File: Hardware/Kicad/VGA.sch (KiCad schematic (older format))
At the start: 9 parts, among them P701 VGA OUT

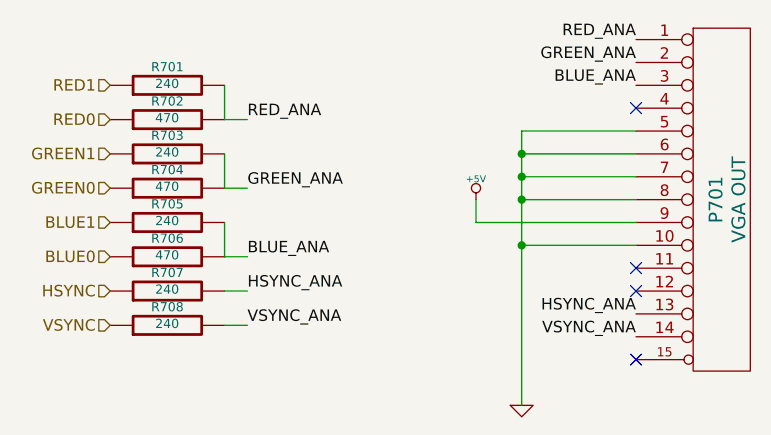
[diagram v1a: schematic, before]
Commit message: Schematic Rev. 11
Added LEDs; some minor other modifications
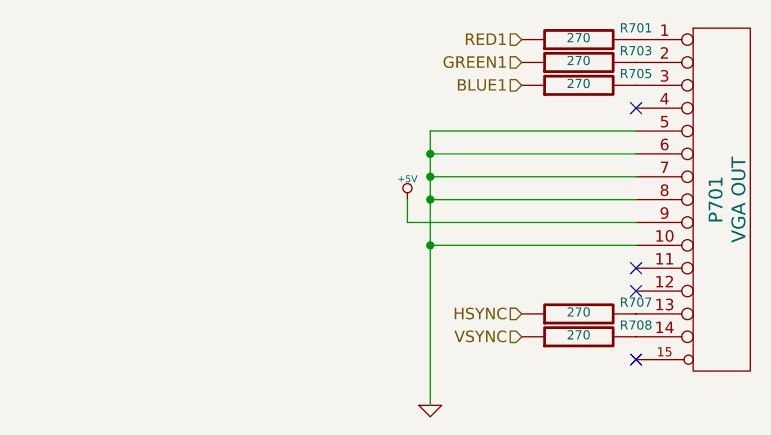
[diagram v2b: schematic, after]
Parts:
- removed R702, R704, R706: 470, ~, symbol R
- R701, R703, R705, R707, R708: value 240 -> 270
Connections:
- net BLUE_ANA: no longer names the net of P701.3 (P3), R705.2
- net GREEN_ANA: no longer names the net of P701.2 (P2), R703.2
- net HSYNC_ANA: no longer names the net of P701.13 (P13), R707.2
- net RED_ANA: no longer names the net of P701.1 (P1), R701.2
- net VSYNC_ANA: no longer names the net of P701.14 (P14), R708.2
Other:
- moved on the sheet: R701, R703, R705, R707, R708
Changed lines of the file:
@@
 Title "Propeddle"
 Date "18 apr 2014"
-Rev "10"
+Rev "11"
 Comp "(C) 2014 Jac Goudsmit"
 Comment1 "Software-Defined 6502 Computer"
@@
 	1    0    0    -1
 $EndComp
-Text Label 6750 3100 2    50   ~ 0
-RED_ANA
-Text Label 6750 3200 2    50   ~ 0
-GREEN_ANA
-Text Label 6750 3300 2    50   ~ 0
-BLUE_ANA
 $Comp
-L GND #PWR031
+L GND #PWR033
 U 1 1 534358FB
-P 6250 4700
-F 0 "#PWR031" H 6250 4700 30  0001 C CNN
-F 1 "GND" H 6250 4630 30  0001 C CNN
-F 2 "" H 6250 4700 60  0000 C CNN
-F 3 "" H 6250 4700 60  0000 C CNN
-	1    6250 4700
+P 5850 4700
+F 0 "#PWR033" H 5850 4700 30  0001 C CNN
+F 1 "GND" H 5850 4630 30  0001 C CNN
+F 2 "" H 5850 4700 60  0000 C CNN
+F 3 "" H 5850 4700 60  0000 C CNN
+	1    5850 4700
 	1    0    0    -1
 $EndComp
 $Comp
-L +5V #PWR032
+L +5V #PWR034
 U 1 1 5343590A
-P 6050 3800
-F 0 "#PWR032" H 6050 3890 20  0001 C CNN
-F 1 "+5V" H 6050 3890 30  0000 C CNN
-F 2 "" H 6050 3800 60  0000 C CNN
-F 3 "" H 6050 3800 60  0000 C CNN
-	1    6050 3800
+P 5750 3800
+F 0 "#PWR034" H 5750 3890 20  0001 C CNN
+F 1 "+5V" H 5750 3890 30  0000 C CNN
+F 2 "" H 5750 3800 60  0000 C CNN
+F 3 "" H 5750 3800 60  0000 C CNN
+	1    5750 3800
 	1    0    0    -1
 $EndComp
-Text Label 6750 4300 2    50   ~ 0
-HSYNC_ANA
-Text Label 6750 4400 2    50   ~ 0
-VSYNC_ANA
 $Comp
 L R R701
 U 1 1 5343593B
-P 4700 3300
-F 0 "R701" V 4780 3300 40  0000 C CNN
-F 1 "240" V 4707 3301 40  0000 C CNN
-F 2 "~" V 4630 3300 30  0000 C CNN
-F 3 "~" H 4700 3300 30  0000 C CNN
-	1    4700 3300
+P 6500 3100
+F 0 "R701" V 6550 2850 40  0000 C CNN
+F 1 "270" V 6507 3101 40  0000 C CNN
+F 2 "~" V 6430 3100 30  0000 C CNN
+F 3 "~" H 6500 3100 30  0000 C CNN
+	1    6500 3100
 	0    -1   -1   0
 $EndComp
@@
 L R R703
 U 1 1 5343594D
-P 4700 3600
-F 0 "R703" V 4780 3600 40  0000 C CNN
-F 1 "240" V 4707 3601 40  0000 C CNN
-F 2 "~" V 4630 3600 30  0000 C CNN
-F 3 "~" H 4700 3600 30  0000 C CNN
-	1    4700 3600
+P 6500 3200
+F 0 "R703" V 6550 2950 40  0000 C CNN
+F 1 "270" V 6507 3201 40  0000 C CNN
+F 2 "~" V 6430 3200 30  0000 C CNN
+F 3 "~" H 6500 3200 30  0000 C CNN
+	1    6500 3200
 	0    -1   -1   0
 $EndComp
@@
 L R R705
 U 1 1 53435953
-P 4700 3900
-F 0 "R705" V 4780 3900 40  0000 C CNN
-F 1 "240" V 4707 3901 40  0000 C CNN
-F 2 "~" V 4630 3900 30  0000 C CNN
-F 3 "~" H 4700 3900 30  0000 C CNN
-	1    4700 3900
-	0    -1   -1   0
-$EndComp
-$Comp
-L R R704
-U 1 1 53435963
-P 4700 3750
-F 0 "R704" V 4780 3750 40  0000 C CNN
-F 1 "470" V 4707 3751 40  0000 C CNN
-F 2 "~" V 4630 3750 30  0000 C CNN
-F 3 "~" H 4700 3750 30  0000 C CNN
-	1    4700 3750
-	0    -1   -1   0
-$EndComp
-$Comp
-L R R702
-U 1 1 5343596E
-P 4700 3450
-F 0 "R702" V 4780 3450 40  0000 C CNN
-F 1 "470" V 4707 3451 40  0000 C CNN
-F 2 "~" V 4630 3450 30  0000 C CNN
-F 3 "~" H 4700 3450 30  0000 C CNN
-	1    4700 3450
-	0    -1   -1   0
-$EndComp
-$Comp
-L R R706
-U 1 1 53435974
-P 4700 4050
-F 0 "R706" V 4780 4050 40  0000 C CNN
-F 1 "470" V 4707 4051 40  0000 C CNN
-F 2 "~" V 4630 4050 30  0000 C CNN
-F 3 "~" H 4700 4050 30  0000 C CNN
-	1    4700 4050
+P 6500 3300
+F 0 "R705" V 6550 3050 40  0000 C CNN
+F 1 "270" V 6507 3301 40  0000 C CNN
+F 2 "~" V 6430 3300 30  0000 C CNN
+F 3 "~" H 6500 3300 30  0000 C CNN
+	1    6500 3300
 	0    -1   -1   0
 $EndComp
@@
 L R R707
 U 1 1 5343597A
-P 4700 4200
-F 0 "R707" V 4780 4200 40  0000 C CNN
-F 1 "240" V 4707 4201 40  0000 C CNN
-F 2 "~" V 4630 4200 30  0000 C CNN
-F 3 "~" H 4700 4200 30  0000 C CNN
-	1    4700 4200
+P 6500 4300
+F 0 "R707" V 6550 4050 40  0000 C CNN
+F 1 "270" V 6507 4301 40  0000 C CNN
+F 2 "~" V 6430 4300 30  0000 C CNN
+F 3 "~" H 6500 4300 30  0000 C CNN
+	1    6500 4300
 	0    -1   -1   0
 $EndComp
@@
 L R R708
 U 1 1 53435980
-P 4700 4350
-F 0 "R708" V 4780 4350 40  0000 C CNN
-F 1 "240" V 4707 4351 40  0000 C CNN
-F 2 "~" V 4630 4350 30  0000 C CNN
-F 3 "~" H 4700 4350 30  0000 C CNN
-	1    4700 4350
+P 6500 4400
+F 0 "R708" V 6550 4150 40  0000 C CNN
+F 1 "270" V 6507 4401 40  0000 C CNN
+F 2 "~" V 6430 4400 30  0000 C CNN
+F 3 "~" H 6500 4400 30  0000 C CNN
+	1    6500 4400
 	0    -1   -1   0
 $EndComp
 Wire Wire Line
-	6750 3500 6250 3500
+	6750 3500 5850 3500
 Wire Wire Line
-	6250 3500 6250 4700
+	5850 3500 5850 4700
 Wire Wire Line
-	6750 4000 6250 4000
-Connection ~ 6250 4000
+	6750 4000 5850 4000
+Connection ~ 5850 4000
 Wire Wire Line
-	6050 3800 6050 3900
+	5750 3800 5750 3900
 Wire Wire Line
-	6050 3900 6750 3900
+	5750 3900 6750 3900
 Wire Wire Line
-	6250 3600 6750 3600
-Connection ~ 6250 3600
+	5850 3600 6750 3600
+Connection ~ 5850 3600
 Wire Wire Line
-	6250 3700 6750 3700
-Connection ~ 6250 3700
+	5850 3700 6750 3700
+Connection ~ 5850 3700
 Wire Wire Line
-	6750 3800 6250 3800
-Connection ~ 6250 3800
-Wire Wire Line
-	4950 3300 4950 3450
-Wire Wire Line
-	4950 3450 5050 3450
-Wire Wire Line
-	4950 3600 4950 3750
-Wire Wire Line
-	4950 3750 5050 3750
-Wire Wire Line
-	4950 3900 4950 4050
-Wire Wire Line
-	4950 4050 5050 4050
-Text Label 5050 3450 0    50   ~ 0
-RED_ANA
-Text Label 5050 3750 0    50   ~ 0
-GREEN_ANA
-Text Label 5050 4050 0    50   ~ 0
-BLUE_ANA
-Wire Wire Line
-	4950 4200 5050 4200
-Wire Wire Line
-	4950 4350 5050 4350
-Text Label 5050 4200 0    50   ~ 0
-HSYNC_ANA
-Text Label 5050 4350 0    50   ~ 0
-VSYNC_ANA
-Text HLabel 4450 3300 0    50   Input ~ 0
+	6750 3800 5850 3800
+Connection ~ 5850 3800
+Text HLabel 6250 3100 0    50   Input ~ 0
 RED1
-Text HLabel 4450 3450 0    50   Input ~ 0
-RED0
-Text HLabel 4450 3600 0    50   Input ~ 0
+Text HLabel 6250 3200 0    50   Input ~ 0
 GREEN1
-Text HLabel 4450 3750 0    50   Input ~ 0
-GREEN0
-Text HLabel 4450 3900 0    50   Input ~ 0
+Text HLabel 6250 3300 0    50   Input ~ 0
 BLUE1
-Text HLabel 4450 4050 0    50   Input ~ 0
-BLUE0
-Text HLabel 4450 4200 0    50   Input ~ 0
+Text HLabel 6250 4300 0    50   Input ~ 0
 HSYNC
-Text HLabel 4450 4350 0    50   Input ~ 0
+Text HLabel 6250 4400 0    50   Input ~ 0
 VSYNC
 NoConn ~ 6750 3400
